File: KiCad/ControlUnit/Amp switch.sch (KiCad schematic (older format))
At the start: 15 parts, among them P17 CONN_01X01, P18 CONN_01X02, P19 CONN_01X01, P20 CONN_01X02, P21 CONN_01X01, P22 CONN_01X02, Q1 2N7002, Q2 2N7002, Q3 2N7002

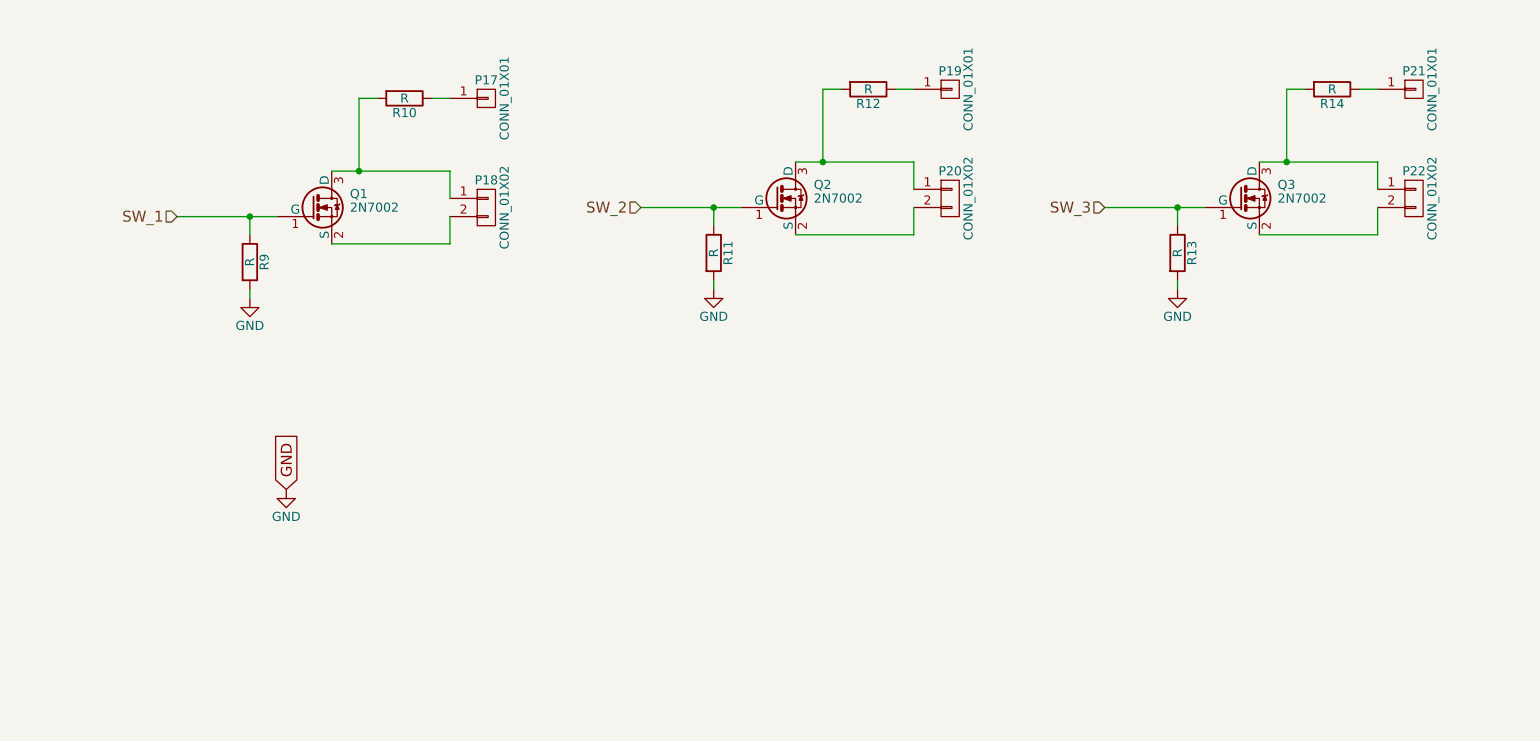
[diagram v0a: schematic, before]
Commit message: Added software for the prototype and made a netlist with footprints for the control unit board
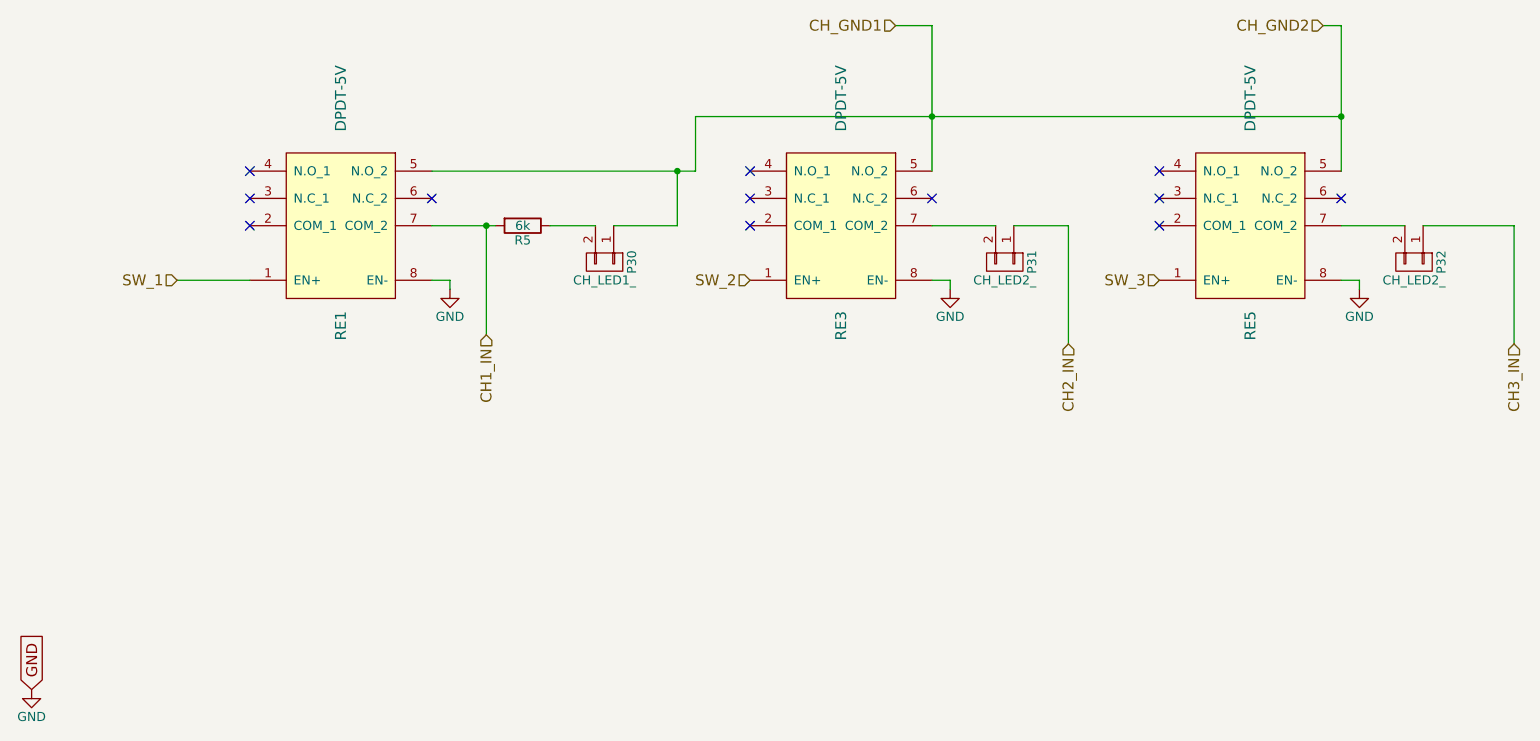
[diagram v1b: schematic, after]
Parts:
- removed P17, P19, P21: CONN_01X01, symbol CONN_01X01
- removed P18, P20, P22: CONN_01X02, symbol CONN_01X02
- removed Q1, Q2, Q3: 2N7002, TO_SOT_Packages_SMD:SOT-23, symbol 2N7002
- removed R10, R11, R12, R13, R14, R9: R, symbol R
- added P30: CH_LED1_, Pin_Headers:Pin_Header_Straight_1x02, symbol CONN_01X02
- added P31, P32: CH_LED2_, Pin_Headers:Pin_Header_Straight_1x02, symbol CONN_01X02
- added R5: 6k, Resistors_ThroughHole:Resistor_Vertical_RM5mm, symbol R
- added RE1, RE3, RE5: DPDT-5V, FroLib:DS2Y_PAK, symbol DPDT-5V
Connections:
- net GND: now also RE1.8 (EN-), RE3.8 (EN-), RE5.8 (EN-)
- net SW_1: now also RE1.1 (EN+)
- net SW_2: now also RE3.1 (EN+)
- net SW_3: now also RE5.1 (EN+)
- new net: P30.2 (P2), R5.1
- new net: P31.2 (P2), RE3.7 (COM_2)
- new net: P32.2 (P2), RE5.7 (COM_2)
- new net CH1_IN: R5.2, RE1.7 (COM_2)
- new net CH2_IN: P31.1 (P1)
- new net CH3_IN: P32.1 (P1)
- new net CH_GND1: P30.1 (P1), RE1.5 (N.O_2), RE3.5 (N.O_2), RE5.5 (N.O_2)
- no-connect marks 0 -> 12

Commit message: Fine tuned PCB design and added multicontact connectors instead of  single connectors
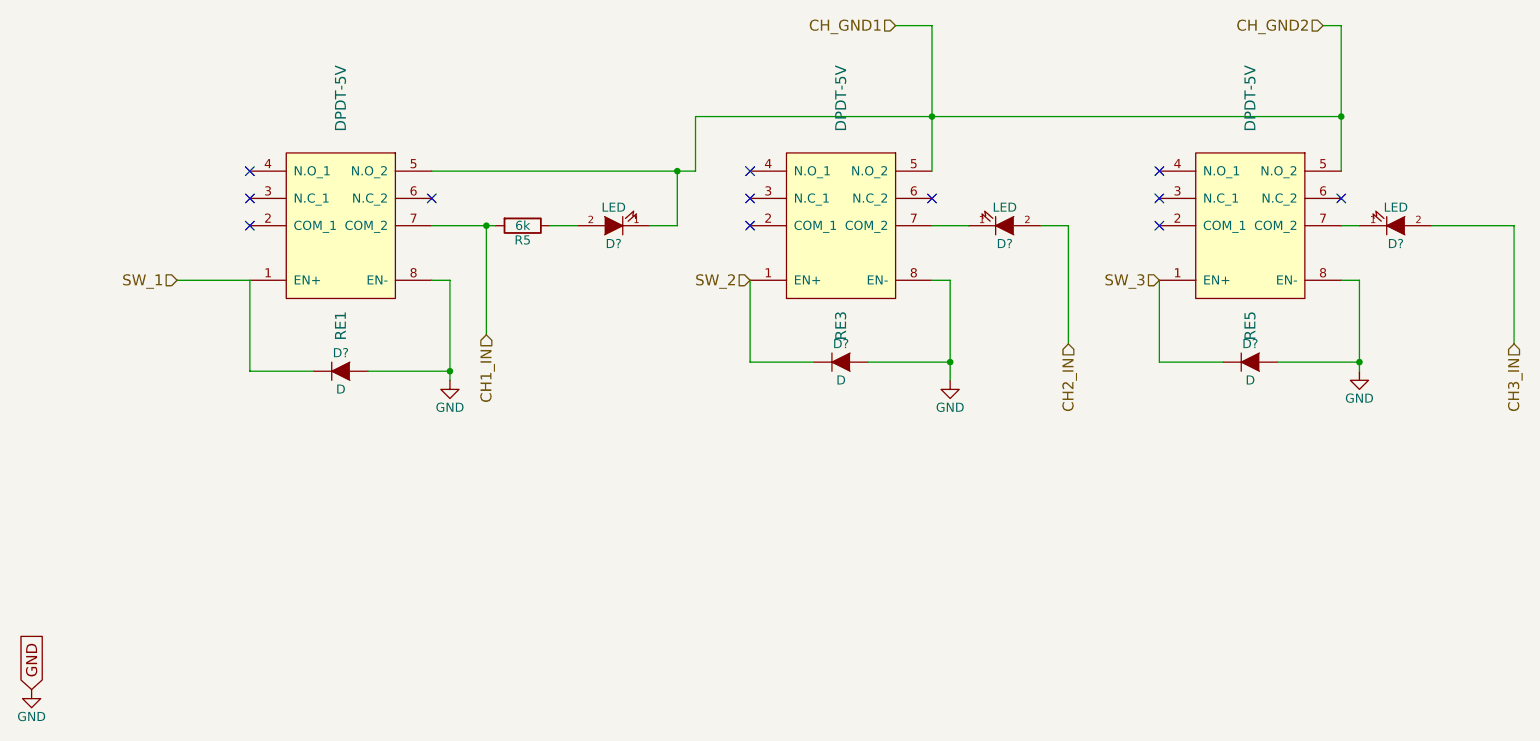
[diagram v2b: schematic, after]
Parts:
- removed P30: CH_LED1_, Pin_Headers:Pin_Header_Straight_1x02, symbol CONN_01X02
- removed P31, P32: CH_LED2_, Pin_Headers:Pin_Header_Straight_1x02, symbol CONN_01X02
- added D? (x3): LED, symbol LED
- added D? (x3): D, symbol D
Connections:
- net CH2_IN: now also D?.2 (A)
- net CH3_IN: now also D?.2 (A)
- net CH_GND1: now also D?.1 (K)
- net GND: now also D?.2 (A), D?.2 (A), D?.2 (A)
- net SW_1: now also D?.1 (K)
- net SW_2: now also D?.1 (K)
- net SW_3: now also D?.1 (K)
- net at R5.1: now also D?.2 (A)
- net at RE3.7 (COM_2): now also D?.1 (K)
- net at RE5.7 (COM_2): now also D?.1 (K)
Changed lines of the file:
@@
 L GND #PWR026
 U 1 1 581881F6
-P 3900 4050
-F 0 "#PWR026" H 3900 3800 50  0001 C CNN
-F 1 "GND" H 3900 3900 50  0000 C CNN
-F 2 "" H 3900 4050 50  0000 C CNN
-F 3 "" H 3900 4050 50  0000 C CNN
-	1    3900 4050
+P 3900 4550
+F 0 "#PWR026" H 3900 4300 50  0001 C CNN
+F 1 "GND" H 3900 4400 50  0000 C CNN
+F 2 "" H 3900 4550 50  0000 C CNN
+F 3 "" H 3900 4550 50  0000 C CNN
+	1    3900 4550
 	1    0    0    -1
 $EndComp
@@
 	2400 4000 2800 4000
 Wire Wire Line
-	3800 4000 3900 4000
-Wire Wire Line
-	3900 4000 3900 4050
+	3900 4000 3900 4550
 $Comp
 L R R5
@@
 	0    1    1    0
 $EndComp
-$Comp
-L CONN_01X02 P30
-U 1 1 5853A8DF
-P 4750 3900
-F 0 "P30" H 4750 4050 50  0000 C CNN
-F 1 "CH_LED1_" V 4850 3900 50  0000 C CNN
-F 2 "Pin_Headers:Pin_Header_Straight_1x02" H 4750 3900 50  0001 C CNN
-F 3 "" H 4750 3900 50  0000 C CNN
-	1    4750 3900
-	0    1    1    0
-$EndComp
 Wire Wire Line
 	3800 3700 4150 3700
 Wire Wire Line
-	4450 3700 4700 3700
+	4450 3700 4600 3700
 $Comp
 L DPDT-5V RE3
@@
 SW_2
 Wire Wire Line
-	4800 3700 5150 3700
+	5000 3700 5150 3700
 Wire Wire Line
 	5150 3700 5150 3400
@@
 	8800 2600 8800 3400
 Connection ~ 6550 3100
-$Comp
-L CONN_01X02 P31
-U 1 1 5853AB9F
-P 6950 3900
-F 0 "P31" H 6950 4050 50  0000 C CNN
-F 1 "CH_LED2_" V 7050 3900 50  0000 C CNN
-F 2 "Pin_Headers:Pin_Header_Straight_1x02" H 6950 3900 50  0001 C CNN
-F 3 "" H 6950 3900 50  0000 C CNN
-	1    6950 3900
-	0    1    1    0
-$EndComp
-Wire Wire Line
-	6550 3700 6900 3700
-$Comp
-L CONN_01X02 P32
-U 1 1 5853AC38
-P 9200 3900
-F 0 "P32" H 9200 4050 50  0000 C CNN
-F 1 "CH_LED2_" V 9300 3900 50  0000 C CNN
-F 2 "Pin_Headers:Pin_Header_Straight_1x02" H 9200 3900 50  0001 C CNN
-F 3 "" H 9200 3900 50  0000 C CNN
-	1    9200 3900
-	0    1    1    0
-$EndComp
-Wire Wire Line
-	8800 3700 9150 3700
+Wire Wire Line
+	6550 3700 6750 3700
+Wire Wire Line
+	8800 3700 8900 3700
 $Comp
 L GND #PWR028
 U 1 1 5853AC93
-P 6650 4050
-F 0 "#PWR028" H 6650 3800 50  0001 C CNN
-F 1 "GND" H 6650 3900 50  0000 C CNN
-F 2 "" H 6650 4050 50  0000 C CNN
-F 3 "" H 6650 4050 50  0000 C CNN
-	1    6650 4050
+P 6650 4550
+F 0 "#PWR028" H 6650 4300 50  0001 C CNN
+F 1 "GND" H 6650 4400 50  0000 C CNN
+F 2 "" H 6650 4550 50  0000 C CNN
+F 3 "" H 6650 4550 50  0000 C CNN
+	1    6650 4550
 	1    0    0    -1
 $EndComp
@@
 	6550 4000 6650 4000
 Wire Wire Line
-	6650 4000 6650 4050
-$Comp
-L GND #PWR029
-U 1 1 5853ACCC
-P 8900 4050
-F 0 "#PWR029" H 8900 3800 50  0001 C CNN
-F 1 "GND" H 8900 3900 50  0000 C CNN
-F 2 "" H 8900 4050 50  0000 C CNN
-F 3 "" H 8900 4050 50  0000 C CNN
-	1    8900 4050
-	1    0    0    -1
-$EndComp
+	6650 4000 6650 4550
 Wire Wire Line
 	8800 4000 8900 4000
 Wire Wire Line
-	8900 4000 8900 4050
+	8900 4000 8900 4500
 Text HLabel 4100 4300 3    60   Input ~ 0
 CH1_IN
@@
 CH2_IN
 Wire Wire Line
-	7000 3700 7300 3700
+	7150 3700 7300 3700
 Wire Wire Line
 	7300 3700 7300 4350
@@
 CH3_IN
 Wire Wire Line
-	9250 3700 9750 3700
+	9300 3700 9750 3700
 Wire Wire Line
 	9750 3700 9750 4350
@@
 	8700 2600 8800 2600
 Connection ~ 8800 3100
+$Comp
+L LED D?
+U 1 1 5875E037
+P 4800 3700
+F 0 "D?" H 4800 3800 50  0000 C CNN
+F 1 "LED" H 4800 3600 50  0000 C CNN
+F 2 "" H 4800 3700 50  0000 C CNN
+F 3 "" H 4800 3700 50  0000 C CNN
+	1    4800 3700
+	-1   0    0    1
+$EndComp
+$Comp
+L LED D?
+U 1 1 5875E142
+P 6950 3700
+F 0 "D?" H 6950 3800 50  0000 C CNN
+F 1 "LED" H 6950 3600 50  0000 C CNN
+F 2 "" H 6950 3700 50  0000 C CNN
+F 3 "" H 6950 3700 50  0000 C CNN
+	1    6950 3700
+	1    0    0    1
+$EndComp
+$Comp
+L LED D?
+U 1 1 5875E272
+P 9100 3700
+F 0 "D?" H 9100 3800 50  0000 C CNN
+F 1 "LED" H 9100 3600 50  0000 C CNN
+F 2 "" H 9100 3700 50  0000 C CNN
+F 3 "" H 9100 3700 50  0000 C CNN
+	1    9100 3700
+	1    0    0    1
+$EndComp
+$Comp
+L D D?
+U 1 1 58774E0C
+P 3300 4500
+F 0 "D?" H 3300 4600 50  0000 C CNN
+F 1 "D" H 3300 4400 50  0000 C CNN
+F 2 "" H 3300 4500 50  0000 C CNN
+F 3 "" H 3300 4500 50  0000 C CNN
+	1    3300 4500
+	1    0    0    -1
+$EndComp
+Wire Wire Line
+	2800 4000 2800 4500
+Wire Wire Line
+	2800 4500 3150 4500
+Wire Wire Line
+	3900 4000 3800 4000
+Wire Wire Line
+	3450 4500 3900 4500
+Connection ~ 3900 4500
+$Comp
+L D D?
+U 1 1 587751AB
+P 6050 4450
+F 0 "D?" H 6050 4550 50  0000 C CNN
+F 1 "D" H 6050 4350 50  0000 C CNN
+F 2 "" H 6050 4450 50  0000 C CNN
+F 3 "" H 6050 4450 50  0000 C CNN
+	1    6050 4450
+	1    0    0    -1
+$EndComp
+$Comp
+L D D?
+U 1 1 587751FC
+P 8300 4450
+F 0 "D?" H 8300 4550 50  0000 C CNN
+F 1 "D" H 8300 4350 50  0000 C CNN
+F 2 "" H 8300 4450 50  0000 C CNN
+F 3 "" H 8300 4450 50  0000 C CNN
+	1    8300 4450
+	1    0    0    -1
+$EndComp
+$Comp
+L GND #PWR?
+U 1 1 5877524E
+P 8900 4500
+F 0 "#PWR?" H 8900 4250 50  0001 C CNN
+F 1 "GND" H 8900 4350 50  0000 C CNN
+F 2 "" H 8900 4500 50  0000 C CNN
+F 3 "" H 8900 4500 50  0000 C CNN
+	1    8900 4500
+	1    0    0    -1
+$EndComp
+Wire Wire Line
+	8900 4450 8450 4450
+Connection ~ 8900 4450
+Wire Wire Line
+	7800 4000 7800 4450
+Wire Wire Line
+	7800 4450 8150 4450
+Wire Wire Line
+	5550 4000 5550 4450
+Wire Wire Line
+	5550 4450 5900 4450
+Wire Wire Line
+	6200 4450 6650 4450
+Connection ~ 6650 4450
 $EndSCHEMATC
